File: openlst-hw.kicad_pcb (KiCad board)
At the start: 4 copper layers, 80 x 80 mm, 166 parts, among them J1 CC Prog/Debug, J10 MS UART1, J11 EXT VBAT, J12 EXT 5V, J13 EXT VRF, J14 EXT 3V3, J15 Conn_02x24_Odd_Even, J2 UART0, J3 Control Outputs, J4 Control Outputs, J5 ANT, J6 Switch Select, J7 Conn_Coaxial, J8 MS UART0, J9 MS Prog/Debug, U1 CC1110, U10 AP63205WU, U11 AP63203WU, U12 AP63200WU, U2 MIC803, U3 SF2446E, U4 PE4250MLI, U5 PE4250MLI, U6 0433BM15A0001, U7 RFFM6406, U8 MSPM0G3107SDGS20R, U9 TJA1051TK-3, X1 TG2520SMN 27MHz

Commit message: ???
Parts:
- renumbered C39 to C37, C37 to C38, C38 to C39
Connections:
- J15 pad 3: unconnected-(J15-Pin_3-Pad3) -> BATT
- J15 pad 37: GND -> /INTERBOARD_CONNECTOR2/5V0_2
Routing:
- net BATT: track 17.8 -> 20.4 mm
- net /INTERBOARD_CONNECTOR2/5V0_2: track 0.00 -> 2.54 mm
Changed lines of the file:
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@@
 	(net 107 "/INTERBOARD_CONNECTOR2/3V3_9")
 	(net 108 "/INTERBOARD_CONNECTOR2/5V0_2")
-	(net 109 "/INTERBOARD_CONNECTOR2/CAN2H")
-	(net 110 "/INTERBOARD_CONNECTOR2/CAN2L")
+	(net 109 "/INTERBOARD_CONNECTOR2/CAN2L")
+	(net 110 "unconnected-(J15-Pin_48-Pad48)")
 	(net 111 "LED1")
 	(net 112 "LED2")
@@
 	(net 127 "Net-(J6-Pin_3)")
 	(net 128 "unconnected-(J15-Pin_1-Pad1)")
-	(net 129 "unconnected-(J15-Pin_47-Pad47)")
-	(net 130 "unconnected-(J15-Pin_3-Pad3)")
-	(net 131 "unconnected-(J15-Pin_48-Pad48)")
-	(net 132 "unconnected-(J15-Pin_2-Pad2)")
-	(net 133 "Net-(U8-PA2_ROSC)")
-	(net 134 "Net-(U7-SAW2)")
-	(net 135 "Net-(U7-SAW1)")
-	(net 136 "unconnected-(U7-NC-Pad25)")
-	(net 137 "unconnected-(U7-NC-Pad14)")
-	(net 138 "unconnected-(U7-NC-Pad16)")
-	(net 139 "unconnected-(U8-PA12_FCC_IN-Pad13)")
+	(net 129 "/INTERBOARD_CONNECTOR2/CAN2H")
+	(net 130 "unconnected-(J15-Pin_47-Pad47)")
+	(net 131 "unconnected-(J15-Pin_2-Pad2)")
+	(net 132 "Net-(U8-PA2_ROSC)")
+	(net 133 "Net-(U7-SAW2)")
+	(net 134 "Net-(U7-SAW1)")
+	(net 135 "unconnected-(U7-NC-Pad25)")
+	(net 136 "unconnected-(U7-NC-Pad14)")
+	(net 137 "unconnected-(U7-NC-Pad16)")
+	(net 138 "unconnected-(U8-PA12_FCC_IN-Pad13)")
 	(footprint "Project:MountingHole_4.3mm_M4_Pad_Via_Custom"
 		(locked yes)
@@
 		(tags "Through hole pin header THT 2x24 2.54mm double row")
 		(property "Reference" "J15"
-			(at -0.57 -2.14 0)
+			(at -0.43 -2.18 0)
 			(layer "F.SilkS")
 			(effects
 				(font
-					(size 0.8 0.6)
+					(size 1 1)
 					(thickness 0.15)
 				)
@@
 			(layers "*.Cu" "*.Mask")
 			(remove_unused_layers no)
-			(net 132 "unconnected-(J15-Pin_2-Pad2)")
+			(net 131 "unconnected-(J15-Pin_2-Pad2)")
 			(pinfunction "Pin_2")
 			(pintype "passive+no_connect")
@@
 			(layers "*.Cu" "*.Mask")
 			(remove_unused_layers no)
-			(net 130 "unconnected-(J15-Pin_3-Pad3)")
+			(net 82 "BATT")
 			(pinfunction "Pin_3")
-			(pintype "passive+no_connect")
+			(pintype "passive")
 		)
 		(pad "4" thru_hole oval
@@
 			(layers "*.Cu" "*.Mask")
 			(remove_unused_layers no)
-			(net 1 "GND")
+			(net 108 "/INTERBOARD_CONNECTOR2/5V0_2")
 			(pinfunction "Pin_37")
 			(pintype "passive")
@@
 			(net 108 "/INTERBOARD_CONNECTOR2/5V0_2")
 			(pinfunction "Pin_38")
-			(pintype "passive+no_connect")
+			(pintype "passive")
 		)
 		(pad "39" thru_hole oval
@@
 			(layers "*.Cu" "*.Mask")
 			(remove_unused_layers no)
-			(net 110 "/INTERBOARD_CONNECTOR2/CAN2L")
+			(net 109 "/INTERBOARD_CONNECTOR2/CAN2L")
 			(pinfunction "Pin_45")
 			(pintype "passive+no_connect")
@@
 			(layers "*.Cu" "*.Mask")
 			(remove_unused_layers no)
-			(net 109 "/INTERBOARD_CONNECTOR2/CAN2H")
+			(net 129 "/INTERBOARD_CONNECTOR2/CAN2H")
 			(pinfunction "Pin_46")
 			(pintype "passive+no_connect")
@@
 			(layers "*.Cu" "*.Mask")
 			(remove_unused_layers no)
-			(net 129 "unconnected-(J15-Pin_47-Pad47)")
+			(net 130 "unconnected-(J15-Pin_47-Pad47)")
 			(pinfunction "Pin_47")
 			(pintype "passive+no_connect")
@@
 			(layers "*.Cu" "*.Mask")
 			(remove_unused_layers no)
-			(net 131 "unconnected-(J15-Pin_48-Pad48)")
+			(net 110 "unconnected-(J15-Pin_48-Pad48)")
 			(pinfunction "Pin_48")
 			(pintype "passive+no_connect")
@@
 		(descr "Capacitor SMD 0603 (1608 Metric), square (rectangular) end terminal, IPC_7351 nominal with elongated pad for handsoldering. (Body size source: IPC-SM-782 page 76, https://www.pcb-3d.com/wordpress/wp-content/uploads/ipc-sm-782a_amendment_1_and_2.pdf), generated with kicad-footprint-generator")
 		(tags "capacitor handsolder")
-		(property "Reference" "C39"
+		(property "Reference" "C37"
 			(at 0 -1.43 -90)
 			(layer "F.SilkS")
@@
 			(size 0.4 0.55)
 			(layers "F.Cu" "F.Paste" "F.Mask")
-			(net 135 "Net-(U7-SAW1)")
+			(net 134 "Net-(U7-SAW1)")
 			(pinfunction "SAW1")
 			(pintype "passive")
@@
 			(size 0.4 0.55)
 			(layers "F.Cu" "F.Paste" "F.Mask")
-			(net 134 "Net-(U7-SAW2)")
+			(net 133 "Net-(U7-SAW2)")
 			(pinfunction "SAW2")
 			(pintype "passive")
@@
 			(size 0.4 0.55)
 			(layers "F.Cu" "F.Paste" "F.Mask")
-			(net 137 "unconnected-(U7-NC-Pad14)")
+			(net 136 "unconnected-(U7-NC-Pad14)")
 			(pinfunction "NC")
 			(pintype "passive+no_connect")
@@
 			(size 0.55 0.4)
 			(layers "F.Cu" "F.Paste" "F.Mask")
-			(net 138 "unconnected-(U7-NC-Pad16)")
+			(net 137 "unconnected-(U7-NC-Pad16)")
 			(pinfunction "NC")
 			(pintype "passive+no_connect")
@@
 			(size 0.4 0.55)
 			(layers "F.Cu" "F.Paste" "F.Mask")
-			(net 136 "unconnected-(U7-NC-Pad25)")
+			(net 135 "unconnected-(U7-NC-Pad25)")
 			(pinfunction "NC")
 			(pintype "passive+no_connect")
@@
 			(size 0.81 1.25)
 			(layers "F.Cu" "F.Paste" "F.Mask")
-			(net 134 "Net-(U7-SAW2)")
+			(net 133 "Net-(U7-SAW2)")
 			(pinfunction "RF")
 			(pintype "passive")
@@
 			(size 0.81 1.25)
 			(layers "F.Cu" "F.Paste" "F.Mask")
-			(net 135 "Net-(U7-SAW1)")
+			(net 134 "Net-(U7-SAW1)")
 			(pinfunction "RF")
 			(pintype "passive")
@@
 		(descr "Capacitor SMD 0402 (1005 Metric), square (rectangular) end terminal, IPC_7351 nominal with elongated pad for handsoldering. (Body size source: IPC-SM-782 page 76, https://www.pcb-3d.com/wordpress/wp-content/uploads/ipc-sm-782a_amendment_1_and_2.pdf), generated with kicad-footprint-generator")
 		(tags "capacitor handsolder")
-		(property "Reference" "C37"
+		(property "Reference" "C38"
 			(at 4.15 0.18 180)
 			(layer "F.SilkS")
@@
 			(layers "F.Cu" "F.Paste" "F.Mask")
 			(roundrect_rratio 0.25)
-			(net 133 "Net-(U8-PA2_ROSC)")
+			(net 132 "Net-(U8-PA2_ROSC)")
 			(pintype "passive")
 		)
@@
 		(descr "Capacitor SMD 0603 (1608 Metric), square (rectangular) end terminal, IPC_7351 nominal with elongated pad for handsoldering. (Body size source: IPC-SM-782 page 76, https://www.pcb-3d.com/wordpress/wp-content/uploads/ipc-sm-782a_amendment_1_and_2.pdf), generated with kicad-footprint-generator")
 		(tags "capacitor handsolder")
-		(property "Reference" "C38"
+		(property "Reference" "C39"
 			(at 3.92 0.21 0)
 			(layer "F.SilkS")
@@
 			(size 1.45 0.299999)
 			(layers "F.Cu" "F.Paste" "F.Mask")
-			(net 133 "Net-(U8-PA2_ROSC)")
+			(net 132 "Net-(U8-PA2_ROSC)")
 			(pinfunction "PA2_ROSC")
 			(pintype "bidirectional")
@@
 			(size 1.45 0.299999)
 			(layers "F.Cu" "F.Paste" "F.Mask")
-			(net 139 "unconnected-(U8-PA12_FCC_IN-Pad13)")
+			(net 138 "unconnected-(U8-PA12_FCC_IN-Pad13)")
 			(pinfunction "PA12_FCC_IN")
 			(pintype "bidirectional+no_connect")
@@
 	)
 	(segment
+		(start 62 73.34)
+		(end 64.54 73.34)
+		(width 1)
+		(layer "In2.Cu")
+		(net 82)
+	)
+	(segment
 		(start 80.36 68.65)
 		(end 77.08 71.93)
@@
 	)
 	(segment
+		(start 62 116.52)
+		(end 64.54 116.52)
+		(width 1)
+		(layer "B.Cu")
+		(net 108)
+	)
+	(segment
 		(start 84.23 104.849386)
 		(end 84.33 104.749386)
@@
 		(width 0.2)
 		(layer "F.Cu")
-		(net 133)
+		(net 132)
 	)
 	(segment
@@
 		(width 0.2)
 		(layer "F.Cu")
-		(net 133)
+		(net 132)
 	)
 	(segment
@@
 		(width 0.2)
 		(layer "F.Cu")
-		(net 133)
+		(net 132)
 	)
 	(segment
@@
 		(width 0.2)
 		(layer "F.Cu")
-		(net 133)
+		(net 132)
 	)
 	(segment
@@
 		(width 0.2)
 		(layer "F.Cu")
-		(net 133)
+		(net 132)
 	)
 	(segment
@@
 		(width 0.333)
 		(layer "F.Cu")
-		(net 134)
+		(net 133)
 	)
 	(segment
@@
 		(width 0.333)
 		(layer "F.Cu")
-		(net 134)
+		(net 133)
 	)
 	(segment
@@
 		(width 0.333)
 		(layer "F.Cu")
-		(net 134)
+		(net 133)
 	)
 	(segment
@@
 		(width 0.333)
 		(layer "F.Cu")
-		(net 134)
+		(net 133)
 	)
 	(segment
@@
 		(width 0.333)
 		(layer "F.Cu")
-		(net 134)
+		(net 133)
 	)
 	(segment
@@
 		(width 0.333)
 		(layer "F.Cu")
-		(net 135)
+		(net 134)
 	)
 	(segment
@@
 		(width 0.333)
 		(layer "F.Cu")
-		(net 135)
+		(net 134)
 	)
 	(segment
@@
 		(width 0.333)
 		(layer "F.Cu")
-		(net 135)
+		(net 134)
 	)
 	(segment
@@
 		(width 0.333)
 		(layer "F.Cu")
-		(net 135)
+		(net 134)
 	)
 	(segment
@@
 		(width 0.333)
 		(layer "F.Cu")
-		(net 135)
+		(net 134)
 	)
 	(zone

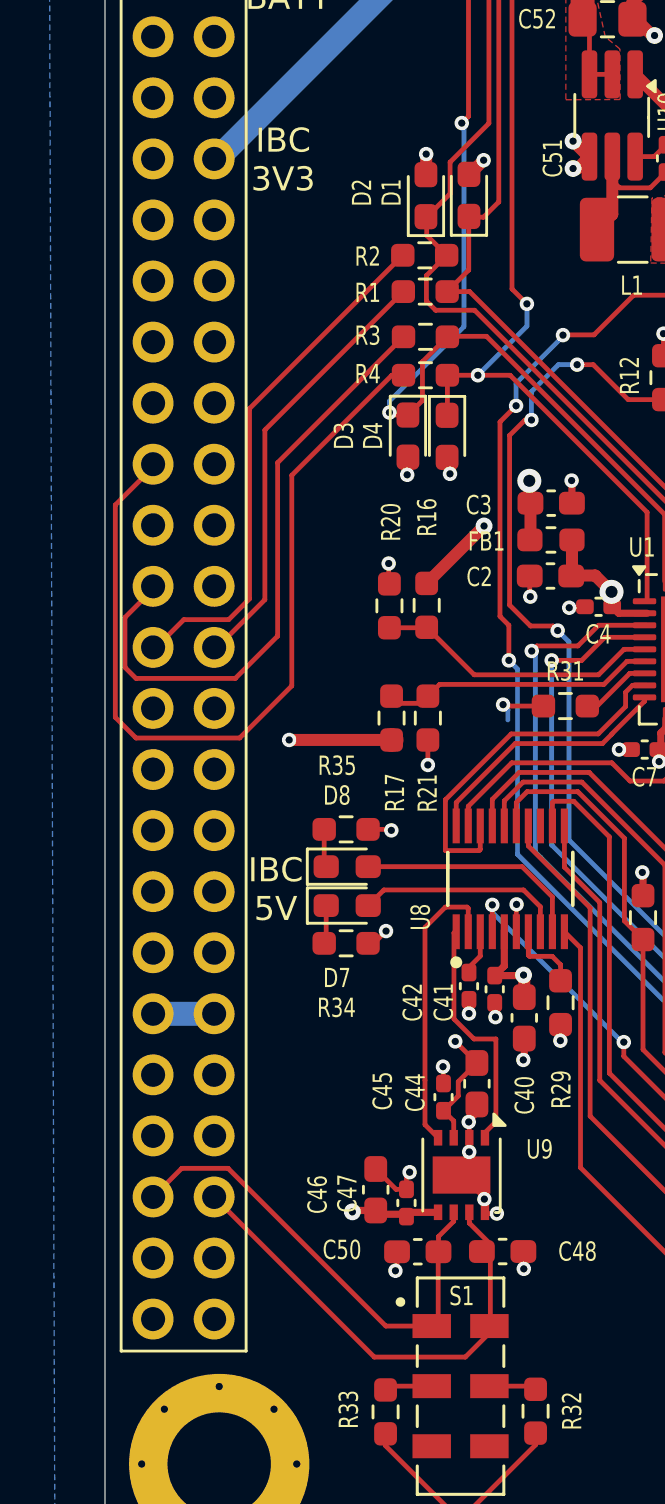
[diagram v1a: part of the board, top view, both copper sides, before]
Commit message: cleanup openlst board after connector update
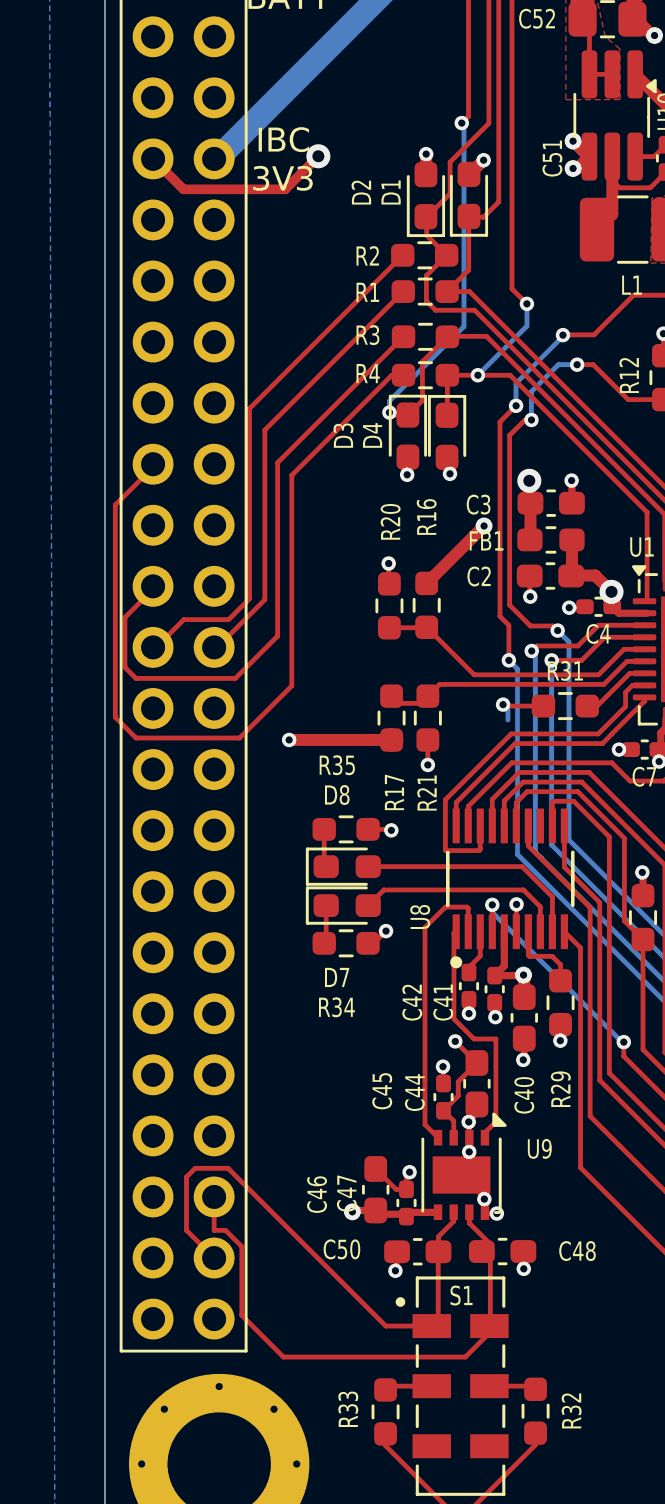
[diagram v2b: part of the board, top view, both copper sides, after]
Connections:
- J15 pad 1: unconnected-(J15-Pin_1-Pad1) -> GND
- J15 pad 11: /INTERBOARD_CONNECTOR2/SPARE_1 -> unconnected-(J15-Pin_11-Pad11)
- J15 pad 12: /INTERBOARD_CONNECTOR2/3V3_7 -> /INTERBOARD_CONNECTOR2/EPS_RESET
- J15 pad 14: GND -> /INTERBOARD_CONNECTOR2/3V3_13
- J15 pad 16: /INTERBOARD_CONNECTOR2/EPS_RESET -> /INTERBOARD_CONNECTOR2/3V3_7
- J15 pad 2: unconnected-(J15-Pin_2-Pad2) -> GND
- J15 pad 31: /INTERBOARD_CONNECTOR2/SPARE_2 -> /INTERBOARD_CONNECTOR2/3V3_4
- J15 pad 33: /INTERBOARD_CONNECTOR2/SPARE_3 -> /INTERBOARD_CONNECTOR2/5V0_2
- J15 pad 34: 5V0 -> /INTERBOARD_CONNECTOR2/SCI_RST
- J15 pad 37: /INTERBOARD_CONNECTOR2/5V0_2 -> /INTERBOARD_CONNECTOR2/5V0_4
- J15 pad 38: /INTERBOARD_CONNECTOR2/5V0_2 -> /INTERBOARD_CONNECTOR2/5V0_3
- J15 pad 39: GND -> unconnected-(J15-Pin_39-Pad39)
- J15 pad 40: /INTERBOARD_CONNECTOR2/SPARE_4 -> /INTERBOARD_CONNECTOR2/3V3_5
- J15 pad 43: CAN_L -> /INTERBOARD_CONNECTOR2/CAN2H
- J15 pad 46: /INTERBOARD_CONNECTOR2/CAN2H -> CAN_L
- J15 pad 47: unconnected-(J15-Pin_47-Pad47) -> GND
- J15 pad 48: unconnected-(J15-Pin_48-Pad48) -> GND
- J15 pad 6: /INTERBOARD_CONNECTOR2/3V3_5 -> /INTERBOARD_CONNECTOR2/2V8_1
- J15 pad 9: /INTERBOARD_CONNECTOR2/3V3_4 -> 5V0
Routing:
- net 5V0: track 53.1 -> 28.8 mm, vias 0 -> 1
- net /INTERBOARD_CONNECTOR2/5V0_2: track 2.54 -> 0.00 mm
- net CAN_H: track 20.0 -> 22.5 mm
- net CAN_L: track 20.1 -> 22.2 mm

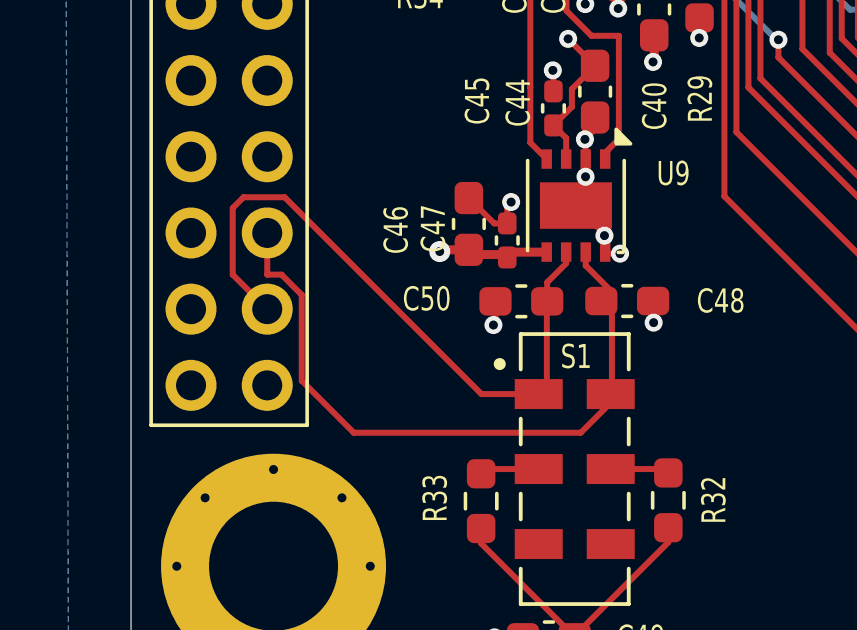
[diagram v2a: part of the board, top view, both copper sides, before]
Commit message: flip can high low around to ease access from front side
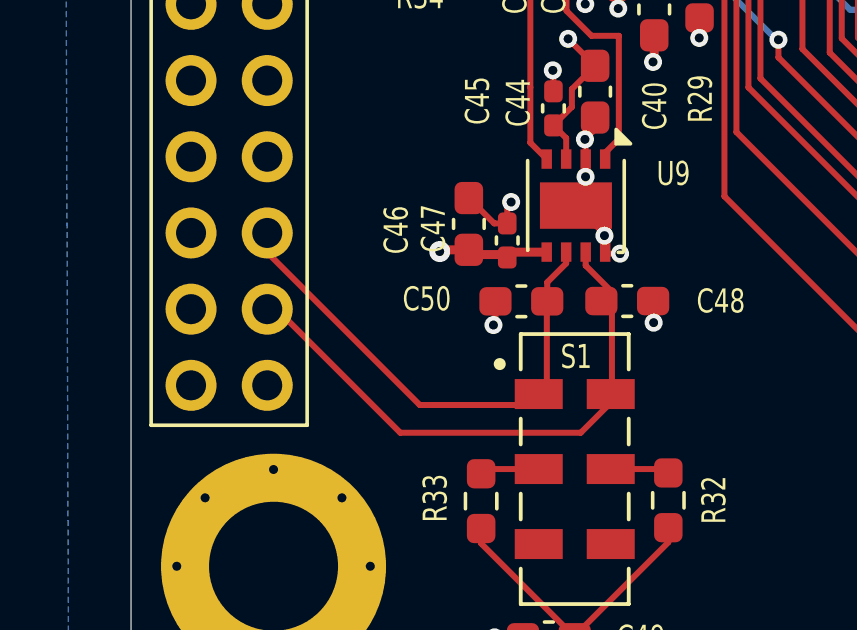
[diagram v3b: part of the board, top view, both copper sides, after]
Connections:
- J15 pad 43: /INTERBOARD_CONNECTOR2/CAN2H -> /INTERBOARD_CONNECTOR2/CAN2L
- J15 pad 44: CAN_H -> CAN_L
- J15 pad 45: /INTERBOARD_CONNECTOR2/CAN2L -> /INTERBOARD_CONNECTOR2/CAN2H
- J15 pad 46: CAN_L -> CAN_H
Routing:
- net CAN_L: track 22.2 -> 17.4 mm
- net CAN_H: track 22.5 -> 19.0 mm
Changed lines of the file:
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@@
 			(layers "*.Cu" "*.Mask")
 			(remove_unused_layers no)
-			(net 129 "/INTERBOARD_CONNECTOR2/CAN2H")
+			(net 109 "/INTERBOARD_CONNECTOR2/CAN2L")
 			(pinfunction "Pin_43")
 			(pintype "passive+no_connect")
@@
 			(layers "*.Cu" "*.Mask")
 			(remove_unused_layers no)
-			(net 42 "CAN_H")
+			(net 41 "CAN_L")
 			(pinfunction "Pin_44")
 			(pintype "passive")
@@
 			(layers "*.Cu" "*.Mask")
 			(remove_unused_layers no)
-			(net 109 "/INTERBOARD_CONNECTOR2/CAN2L")
+			(net 129 "/INTERBOARD_CONNECTOR2/CAN2H")
 			(pinfunction "Pin_45")
 			(pintype "passive+no_connect")
@@
 			(layers "*.Cu" "*.Mask")
 			(remove_unused_layers no)
-			(net 41 "CAN_L")
+			(net 42 "CAN_H")
 			(pinfunction "Pin_46")
 			(pintype "passive")
@@
 	)
 	(segment
-		(start 63.39 123.31)
-		(end 63.75 122.95)
+		(start 64.54 124.14)
+		(end 64.54 124.79)
 		(width 0.2)
 		(layer "F.Cu")
@@
 	)
 	(segment
-		(start 64.54 126.68)
-		(end 63.39 125.53)
-		(width 0.2)
-		(layer "F.Cu")
-		(net 41)
-	)
-	(segment
-		(start 71.68 129.51)
-		(end 73.86 129.51)
+		(start 73.86 126.4325)
+		(end 73.8725 126.42)
 		(width 0.2)
 		(layer "F.Cu")
@@
 	)
 	(segment
-		(start 73.86 126.4325)
-		(end 73.8725 126.42)
-		(width 0.2)
-		(layer "F.Cu")
-		(net 41)
-	)
-	(segment
-		(start 63.75 122.95)
-		(end 65.12 122.95)
+		(start 69.625 129.875)
+		(end 73.86 129.875)
 		(width 0.2)
 		(layer "F.Cu")
@@
 	)
 	(segment
-		(start 73.86 129.51)
-		(end 73.86 126.4325)
+		(start 64.54 124.79)
+		(end 69.625 129.875)
 		(width 0.2)
 		(layer "F.Cu")
@@
 	)
 	(segment
-		(start 63.39 125.53)
-		(end 63.39 123.31)
-		(width 0.2)
-		(layer "F.Cu")
-		(net 41)
-	)
-	(segment
-		(start 65.12 122.95)
-		(end 71.68 129.51)
+		(start 73.86 129.875)
+		(end 73.86 126.4325)
 		(width 0.2)
 		(layer "F.Cu")
@@
 	)
 	(segment
-		(start 74.99 130.8)
-		(end 67.425 130.8)
-		(width 0.2)
-		(layer "F.Cu")
-		(net 42)
-	)
-	(segment
-		(start 65.69 129.065)
-		(end 65.69 126.203654)
-		(width 0.2)
-		(layer "F.Cu")
-		(net 42)
-	)
-	(segment
-		(start 65.69 126.203654)
-		(end 65.016346 125.53)
+		(start 76.03 129.76)
+		(end 74.99 130.8)
 		(width 0.2)
 		(layer "F.Cu")
@@
 	)
 	(segment
-		(start 67.425 130.8)
-		(end 65.69 129.065)
+		(start 68.975 130.8)
+		(end 64.855 126.68)
 		(width 0.2)
 		(layer "F.Cu")
@@
 	)
 	(segment
-		(start 75.155 124.7775)
-		(end 75.155 125.2275)
+		(start 75.155 125.2275)
+		(end 76.03 126.1025)
 		(width 0.2)
 		(layer "F.Cu")
@@
 	)
 	(segment
-		(start 75.155 125.2275)
-		(end 76.03 126.1025)
-		(width 0.2)
-		(layer "F.Cu")
-		(net 42)
-	)
-	(segment
-		(start 76.03 129.76)
-		(end 74.99 130.8)
+		(start 75.155 124.7775)
+		(end 75.155 125.2275)
 		(width 0.2)
 		(layer "F.Cu")
@@
 	)
 	(segment
-		(start 64.54 125.53)
-		(end 64.54 124.14)
+		(start 64.855 126.68)
+		(end 64.54 126.68)
 		(width 0.2)
 		(layer "F.Cu")
@@
 	)
 	(segment
-		(start 65.016346 125.53)
-		(end 64.54 125.53)
+		(start 74.99 130.8)
+		(end 68.975 130.8)
 		(width 0.2)
 		(layer "F.Cu")
